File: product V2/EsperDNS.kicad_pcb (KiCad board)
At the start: 2 copper layers, 49 x 48 mm, 54 parts, among them J1 10118192-0001LF, J2 ARJM11A3, J3 Conn_02x05_Odd_Even, Q1 Q_NMOS_GSD, Q2 Q_NMOS_GSD, Q3 Q_NMOS_GSD, SW1 1-1825027-1, U1 AZ1117-3.3, U2 LAN8720A, U3 ESP32-WROOM-32D

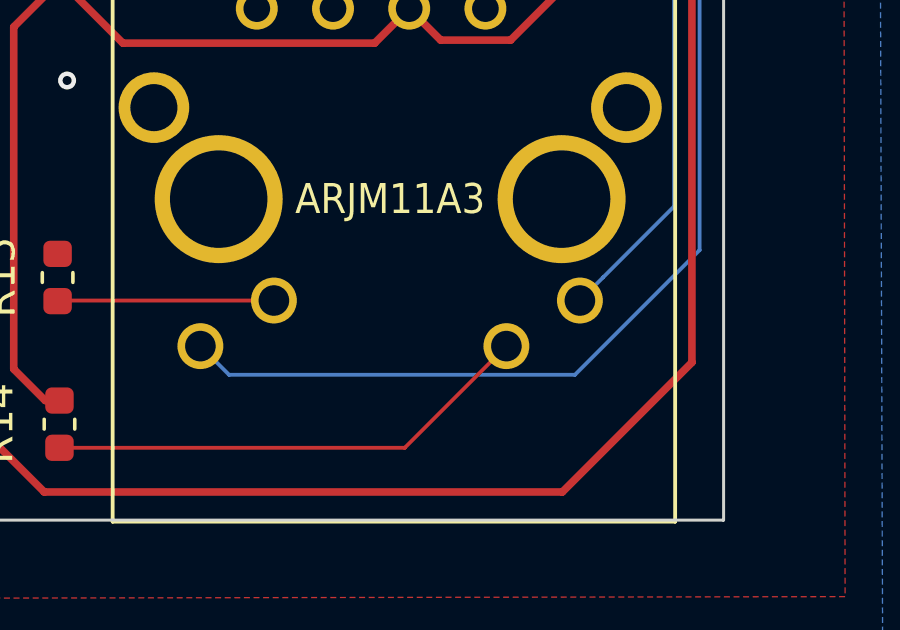
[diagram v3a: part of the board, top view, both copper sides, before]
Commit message: Added buttons and LEDs
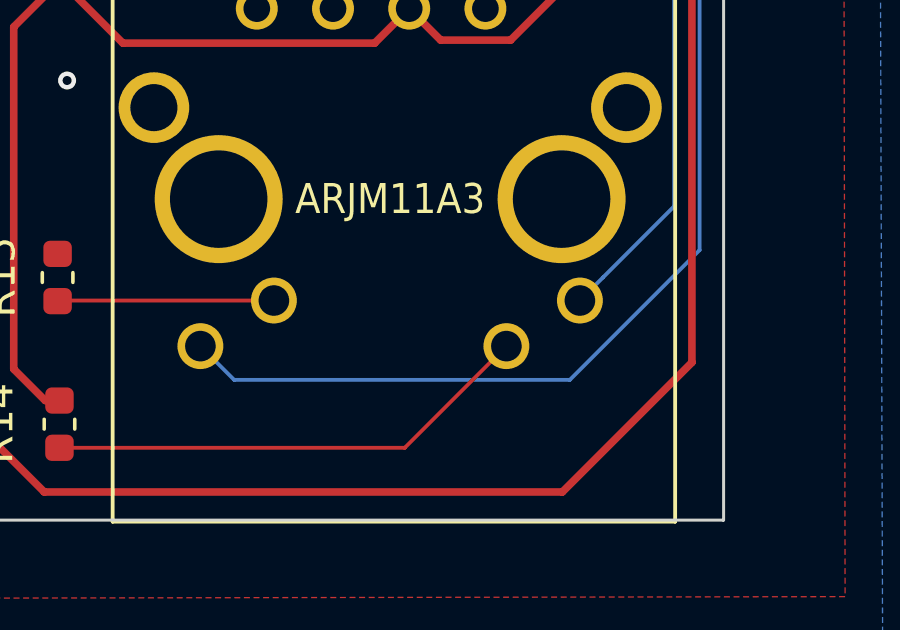
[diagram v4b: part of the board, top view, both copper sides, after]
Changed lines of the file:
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@@
       (drillshape 0)
       (scaleselection 1)
-      (outputdirectory "Gerber Files/"))
+      (outputdirectory "Assembly/"))
   )
   (net 0 "")
@@
   (segment (start 179 92.6625) (end 179 90.475) (width 0.25) (layer F.Cu) (net 15))
   (segment (start 179 90.475) (end 177.8 89.275) (width 0.25) (layer F.Cu) (net 15))
-  (segment (start 181.914 86.614) (end 181.102 86.614) (width 0.127) (layer B.Cu) (net 16))
-  (segment (start 171.515501 111.155501) (end 183.044499 111.155501) (width 0.127) (layer B.Cu) (net 16))
-  (segment (start 187.2 107) (end 187.2 91.9) (width 0.127) (layer B.Cu) (net 16))
-  (segment (start 170.56 110.2) (end 171.515501 111.155501) (width 0.127) (layer B.Cu) (net 16))
-  (segment (start 183.044499 111.155501) (end 187.2 107) (width 0.127) (layer B.Cu) (net 16))
-  (segment (start 187.2 91.9) (end 181.914 86.614) (width 0.127) (layer B.Cu) (net 16))
   (segment (start 181.102 86.614) (end 181.102 86.614) (width 0.127) (layer B.Cu) (net 16))
   (via (at 181.102 86.614) (size 0.6) (drill 0.3) (layers F.Cu B.Cu) (net 16))
@@
   (segment (start 179.4875 86.8) (end 179.6125 86.675) (width 0.127) (layer F.Cu) (net 16))
   (segment (start 179.6125 86.675) (end 180.616736 86.675) (width 0.127) (layer F.Cu) (net 16))
+  (segment (start 181.914 86.614) (end 181.102 86.614) (width 0.127) (layer B.Cu) (net 16))
+  (segment (start 187.2 91.9) (end 181.914 86.614) (width 0.127) (layer B.Cu) (net 16))
+  (segment (start 187.2 107) (end 187.2 91.9) (width 0.127) (layer B.Cu) (net 16))
+  (segment (start 182.875 111.325) (end 187.2 107) (width 0.127) (layer B.Cu) (net 16))
+  (segment (start 170.56 110.2) (end 171.685 111.325) (width 0.127) (layer B.Cu) (net 16))
+  (segment (start 171.685 111.325) (end 182.875 111.325) (width 0.127) (layer B.Cu) (net 16))
   (segment (start 179.4875 87.3) (end 180.55 87.3) (width 0.127) (layer F.Cu) (net 17))
   (segment (start 180.55 87.3) (end 180.55 87.3) (width 0.127) (layer F.Cu) (net 17))
@@
   (zone (net 0) (net_name "") (layers F&B.Cu) (hatch edge 0.508)
     (connect_pads (clearance 0.2032))
-    (min_thickness 0.254)
-    (keepout (tracks allowed) (vias not_allowed) (copperpour not_allowed))
-    (fill (arc_segments 32) (thermal_gap 0.508) (thermal_bridge_width 0.508))
-    (polygon
-      (pts
-        (xy 186.75 116.5) (xy 167.1 116.5) (xy 167.05 101) (xy 167.05 100.55) (xy 186.75 100.55)
-      )
-    )
-  )
-  (zone (net 0) (net_name "") (layers F&B.Cu) (hatch edge 0.508)
-    (connect_pads (clearance 0.2032))

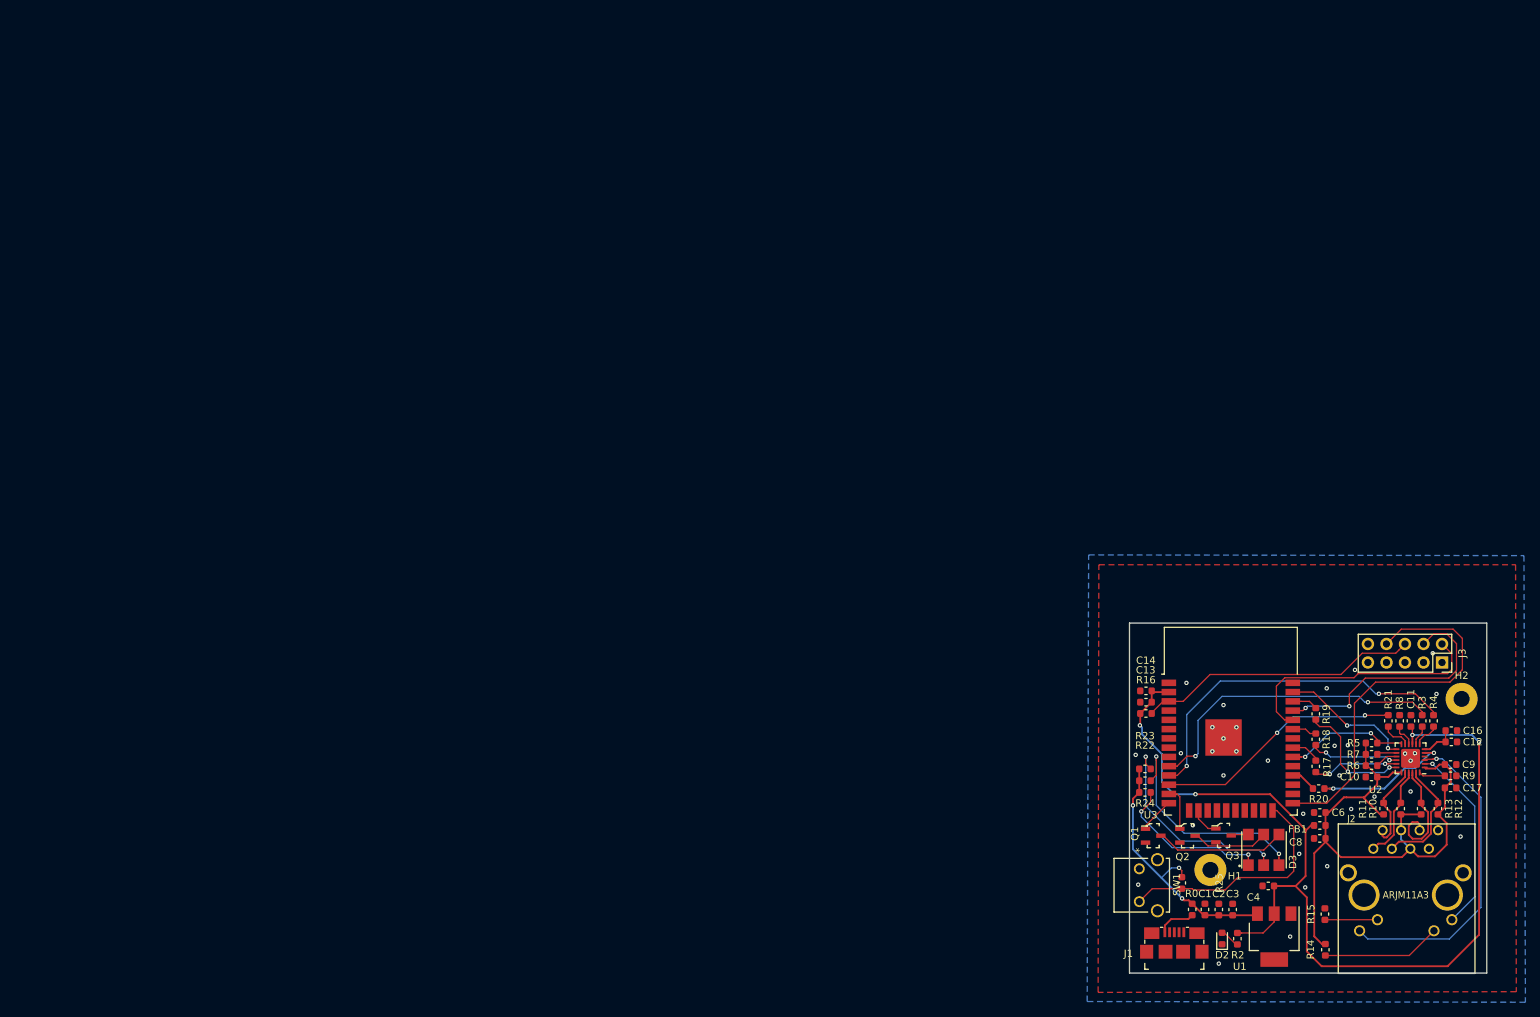
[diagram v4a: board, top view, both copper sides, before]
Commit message: Changed board outline and mounting to better fit inside enclosure
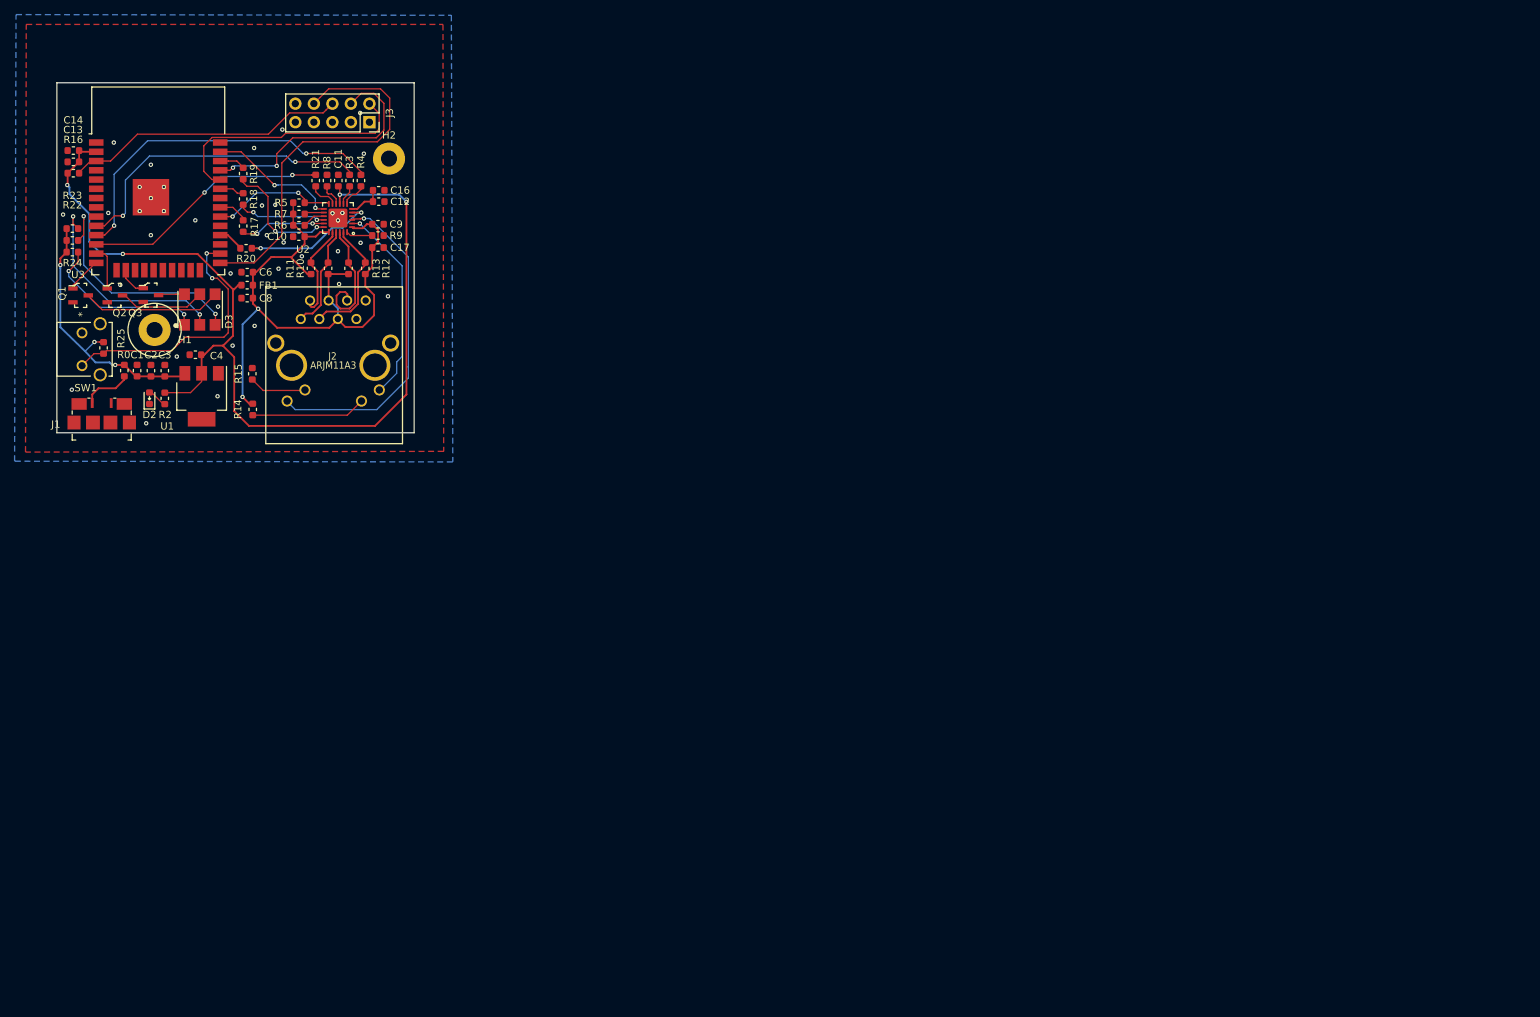
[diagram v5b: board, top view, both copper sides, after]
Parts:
- C4, C6: value 4.7uF -> 10uF
- J1: footprint digikey-footprints:USB_Micro_B_Female_10118192 -> My Footprints:USB_Micro_B_Female_10118192
- R22, R23: value R -> 47
- R24: value R -> 82
- U2: footprint Package_DFN_QFN:QFN-24-1EP_4x4mm_P0.5mm_EP2.6x2.6mm -> My Footprints:QFN-24-1EP_4x4mm_P0.5mm_EP2.6x2.6mm
- moved R25 165.1 mm to (-1.70, 30.3)
- moved H2 164.7 mm to (37.5, 4.30)
- moved Q2 164.7 mm to (-0.14, 23.1)
- moved R12 164.7 mm to (34.2, 19.4)
- moved R15 164.7 mm to (18.7, 33.8)
- moved R17 164.7 mm to (17.4, 13.6)
- moved R18 164.7 mm to (17.4, 9.84)
- moved R19 164.7 mm to (17.4, 6.35)
- moved R2 164.7 mm to (6.70, 37.2)
- moved R3 164.7 mm to (32.0, 7.31)
- moved R8 164.7 mm to (28.9, 7.31)
- moved U2 164.7 mm to (30.4, 12.4)
- moved C10 164.7 mm to (25.1, 15.0)
- moved C11 164.7 mm to (30.5, 7.31)
- moved C12 164.7 mm to (36.0, 10.2)
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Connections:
- U3 pad 24: Block -> Net-(U3-Pad24)
- U3 pad 26: Net-(U3-Pad26) -> Block
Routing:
- net +3V3: track 140.0 -> 136.4 mm
- net AVDD: track 84.7 -> 88.3 mm, vias 0 -> 2
- net Block: track 32.9 -> 36.3 mm, vias 0 -> 2
- net Net-(J1-Pad1): track 5.26 -> 6.86 mm
- net LED1_REGOFF: track 44.0 -> 45.5 mm
- net LED2_nINTSEL: track 26.1 -> 27.7 mm
- net /Page 1/RD+: track 16.3 -> 17.7 mm
- net /Page 1/TD+: track 13.0 -> 14.4 mm
- net /Page 1/RD-: track 16.2 -> 17.6 mm
- net Net-(D3-Pad5): track 10.7 -> 12.0 mm
- net /Page 1/TD-: track 12.2 -> 13.5 mm
- net Net-(D3-Pad3): track 31.5 -> 32.7 mm
- net Net-(D3-Pad6): track 17.9 -> 19.1 mm
- net Net-(D3-Pad2): track 29.1 -> 30.3 mm
- net Net-(D3-Pad4): track 2.40 -> 3.60 mm
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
